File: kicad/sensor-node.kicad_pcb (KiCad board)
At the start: 2 copper layers, 30 x 54 mm, 24 parts

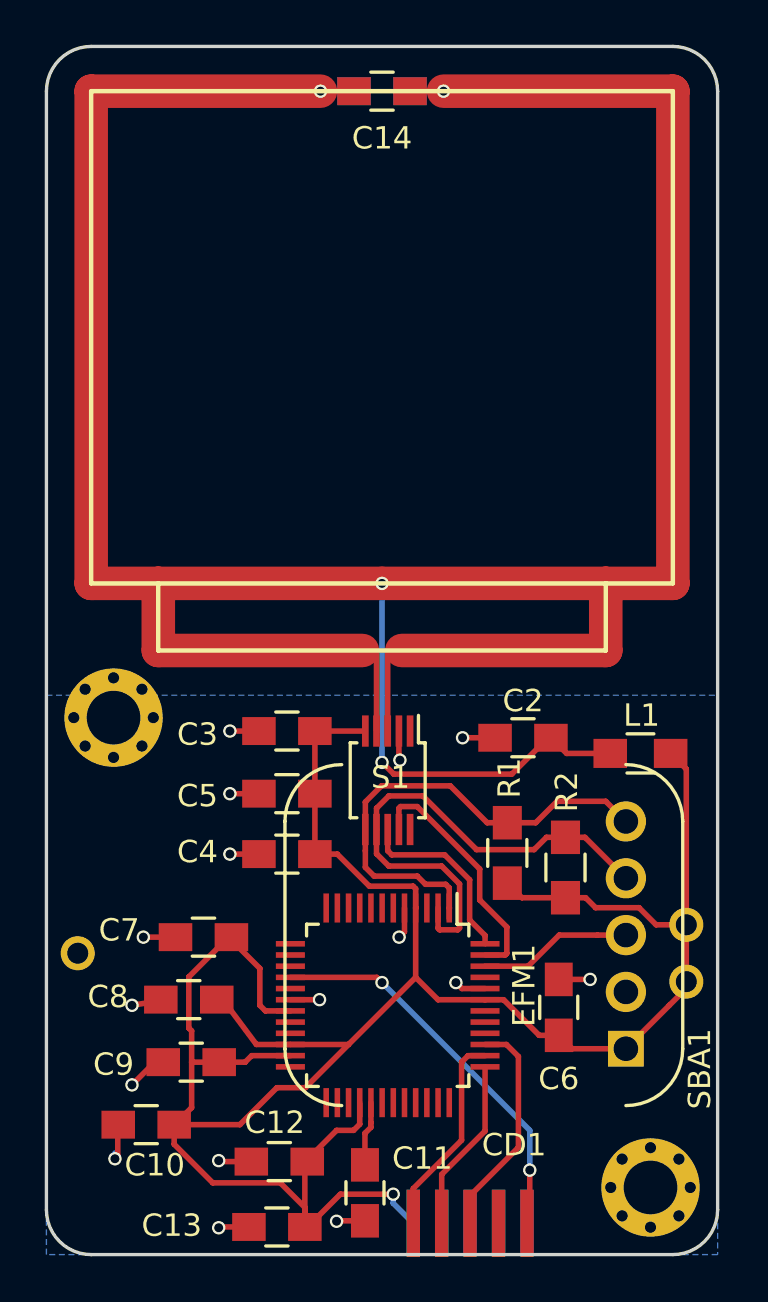
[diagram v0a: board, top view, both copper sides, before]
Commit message: moved cortex debug connector futher to the right
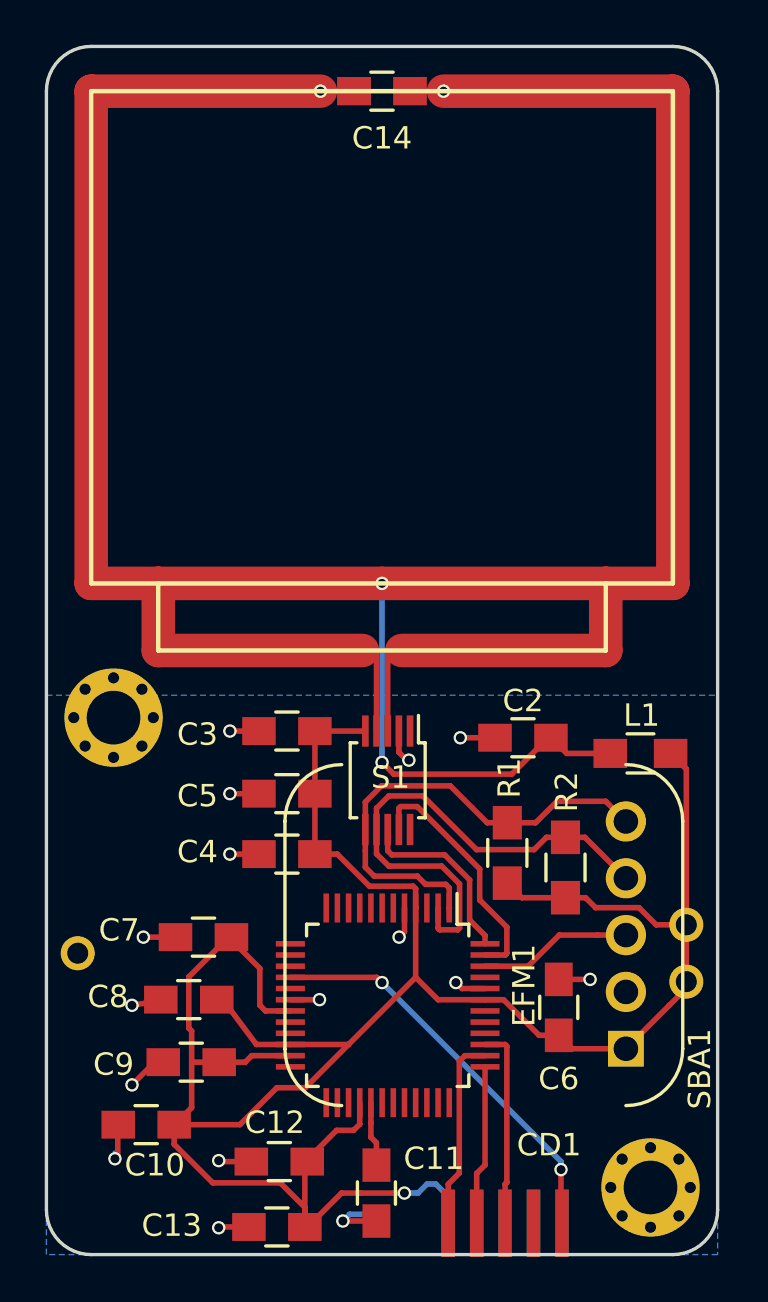
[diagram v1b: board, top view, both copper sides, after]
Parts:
- moved CD1 1.56 mm to (155.1, 110.1)
- moved C11 0.51 mm to (151.9, 108.7)
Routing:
- net +3V3: track 113.5 -> 116.0 mm
- net GND: track 22.9 -> 24.8 mm
- net /SWDIO: track 10.1 -> 8.70 mm
- net /~RESET: track 17.3 -> 18.3 mm
- net /SWO: track 9.85 -> 8.95 mm
- net /SWCLK: track 7.70 -> 7.15 mm

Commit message: moved mounting hole and battery slightliy down
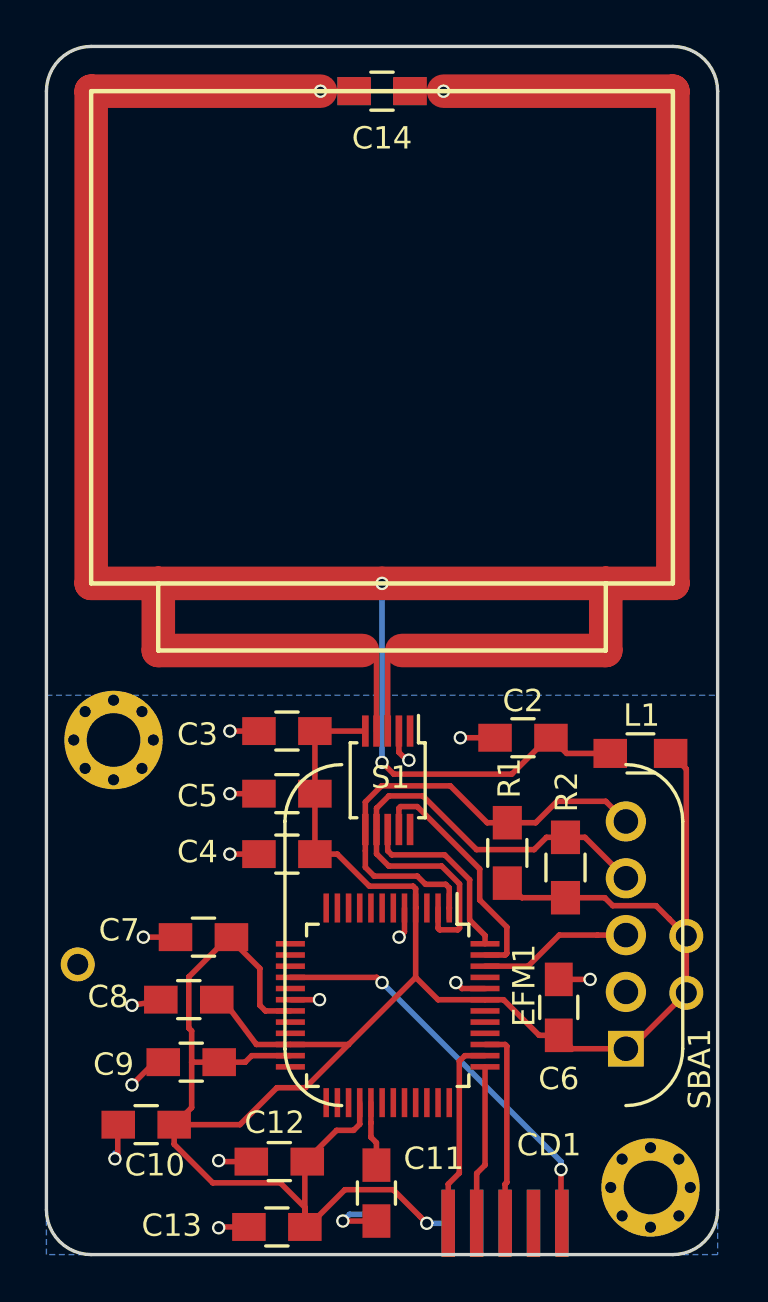
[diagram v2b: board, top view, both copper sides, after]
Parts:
- moved REF** 1.00 mm to (140.1, 88.5)
- moved BT1 0.50 mm to (165.7, 98.5)
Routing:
- net +3V3: track 116.0 -> 115.3 mm
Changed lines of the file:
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@@
     (thickness 1.6)
     (drawings 18)
-    (tracks 242)
+    (tracks 238)
     (zones 0)
     (modules 24)
@@
   )
   (module sensor-node:HU2032-LF (layer B.Cu)
-    (at 165.746 98.001 180)
+    (at 165.746 98.501 180)
     (fp_text reference BT1 (at 13.208 0 180) (layer B.SilkS)
       (effects (font (size 1 1) (thickness 0.15)) (justify mirror))
@@
   )
   (module sensor-node:mounting (layer F.Cu)
-    (at 140.146 87.471)
+    (at 140.146 88.471)
     (fp_text reference REF** (at 0 0.5) (layer F.SilkS) hide
       (effects (font (size 1 1) (thickness 0.15)))
@@
   (gr_line (start 137.146 109.471) (end 137.146 59.471) (layer Edge.Cuts) (width 0.15))
   (gr_line (start 167.146 59.471) (end 167.146 109.471) (layer Edge.Cuts) (width 0.15))
-  (segment (start 153.146 108.721) (end 153.756 108.721) (width 0.25) (layer B.Cu) (net 1))
-  (segment (start 153.756 108.721) (end 154.156 108.321) (width 0.25) (layer B.Cu) (net 1))
-  (segment (start 154.556 108.321) (end 155.106 108.871) (width 0.25) (layer B.Cu) (net 1))
-  (segment (start 154.156 108.321) (end 154.556 108.321) (width 0.25) (layer B.Cu) (net 1))
-  (segment (start 155.106 108.871) (end 155.106 110.071) (width 0.25) (layer B.Cu) (net 1))
-  (segment (start 153.146 108.721) (end 153.216 108.721) (width 0.25) (layer B.Cu) (net 1))
-  (segment (start 148.822 110.236) (end 150.337 108.721) (width 0.25) (layer F.Cu) (net 1))
-  (segment (start 150.337 108.721) (end 151.185998 108.721) (width 0.25) (layer F.Cu) (net 1))
-  (segment (start 151.185998 108.721) (end 153.146 108.721) (width 0.25) (layer F.Cu) (net 1))
-  (via (at 153.146 108.721) (size 0.6) (drill 0.4) (layers F.Cu B.Cu) (net 1))
+  (segment (start 165.746 99.771) (end 165.746 98.69337) (width 0.25) (layer F.Cu) (net 1))
+  (segment (start 165.746 98.69337) (end 165.746 97.231) (width 0.25) (layer F.Cu) (net 1))
+  (segment (start 165.746 99.771) (end 163.246 102.271) (width 0.25) (layer F.Cu) (net 1))
+  (segment (start 163.246 102.271) (end 163.046 102.271) (width 0.25) (layer F.Cu) (net 1))
+  (segment (start 165.746 97.231) (end 165.746 89.771) (width 0.25) (layer F.Cu) (net 1))
+  (segment (start 165.746 89.771) (end 165.046 89.071) (width 0.25) (layer F.Cu) (net 1))
+  (segment (start 160.346 95.521) (end 162.102998 95.521) (width 0.25) (layer F.Cu) (net 1))
+  (segment (start 162.102998 95.521) (end 162.457999 95.876001) (width 0.25) (layer F.Cu) (net 1))
+  (segment (start 162.457999 95.876001) (end 164.391001 95.876001) (width 0.25) (layer F.Cu) (net 1))
+  (segment (start 164.391001 95.876001) (end 164.984001 96.469001) (width 0.25) (layer F.Cu) (net 1))
+  (segment (start 164.984001 96.469001) (end 165.746 97.231) (width 0.25) (layer F.Cu) (net 1))
+  (segment (start 154.146006 110.071) (end 155.106 110.071) (width 0.25) (layer B.Cu) (net 1))
+  (segment (start 153.846007 109.771001) (end 154.146006 110.071) (width 0.25) (layer F.Cu) (net 1))
+  (segment (start 152.645991 108.570985) (end 153.846007 109.771001) (width 0.25) (layer F.Cu) (net 1))
+  (segment (start 150.487015 108.570985) (end 152.645991 108.570985) (width 0.25) (layer F.Cu) (net 1))
+  (segment (start 148.822 110.236) (end 150.487015 108.570985) (width 0.25) (layer F.Cu) (net 1))
+  (segment (start 148.697 110.236) (end 148.822 110.236) (width 0.25) (layer F.Cu) (net 1))
+  (via (at 154.146006 110.071) (size 0.6) (drill 0.4) (layers F.Cu B.Cu) (net 1))
   (segment (start 160.346 95.521) (end 158.398 95.521) (width 0.25) (layer F.Cu) (net 1))
   (segment (start 158.398 95.521) (end 157.746 94.869) (width 0.25) (layer F.Cu) (net 1))
-  (segment (start 165.746 96.731) (end 164.399002 96.731) (width 0.25) (layer F.Cu) (net 1))
-  (segment (start 164.399002 96.731) (end 163.634001 95.965999) (width 0.25) (layer F.Cu) (net 1))
-  (segment (start 163.634001 95.965999) (end 161.690999 95.965999) (width 0.25) (layer F.Cu) (net 1))
-  (segment (start 161.690999 95.965999) (end 161.246 95.521) (width 0.25) (layer F.Cu) (net 1))
-  (segment (start 161.246 95.521) (end 160.346 95.521) (width 0.25) (layer F.Cu) (net 1))
   (segment (start 150.146 93.571) (end 149.146 93.571) (width 0.25) (layer F.Cu) (net 1))
   (segment (start 153.535001 95.004999) (end 151.579999 95.004999) (width 0.25) (layer F.Cu) (net 1))
@@
   (segment (start 153.65 95.98) (end 153.65 95.119998) (width 0.25) (layer F.Cu) (net 1))
   (segment (start 153.65 95.119998) (end 153.535001 95.004999) (width 0.25) (layer F.Cu) (net 1))
-  (segment (start 148.697 110.236) (end 148.822 110.236) (width 0.25) (layer F.Cu) (net 1))
   (segment (start 160.793 95.504) (end 159.893 95.504) (width 0.25) (layer F.Cu) (net 1))
   (segment (start 148.697 110.236) (end 148.697 109.361) (width 0.25) (layer F.Cu) (net 1))
@@
   (segment (start 149.146 90.871) (end 149.146 88.071) (width 0.25) (layer F.Cu) (net 1))
   (segment (start 149.146 93.571) (end 149.146 90.871) (width 0.25) (layer F.Cu) (net 1))
-  (segment (start 165.746 97.031) (end 165.746 89.771) (width 0.25) (layer F.Cu) (net 1))
-  (segment (start 165.746 89.771) (end 165.046 89.071) (width 0.25) (layer F.Cu) (net 1))
-  (segment (start 165.746 99.571) (end 165.746 98.49337) (width 0.25) (layer F.Cu) (net 1))
-  (segment (start 165.746 98.49337) (end 165.746 97.031) (width 0.25) (layer F.Cu) (net 1))
   (segment (start 160.046 101.671) (end 159.171 101.671) (width 0.25) (layer F.Cu) (net 1))
   (segment (start 159.171 101.671) (end 157.58 100.08) (width 0.25) (layer F.Cu) (net 1))
@@
   (segment (start 163.046 102.271) (end 160.646 102.271) (width 0.25) (layer F.Cu) (net 1))
   (segment (start 160.646 102.271) (end 160.046 101.671) (width 0.25) (layer F.Cu) (net 1))
-  (segment (start 165.746 99.571) (end 164.984001 100.332999) (width 0.25) (layer F.Cu) (net 1))
-  (segment (start 164.984001 100.332999) (end 163.046 102.271) (width 0.25) (layer F.Cu) (net 1))
   (segment (start 144.867 102.87) (end 143.637 102.87) (width 0.25) (layer F.Cu) (net 1))
   (segment (start 146.03 102.87) (end 144.867 102.87) (width 0.25) (layer F.Cu) (net 1))

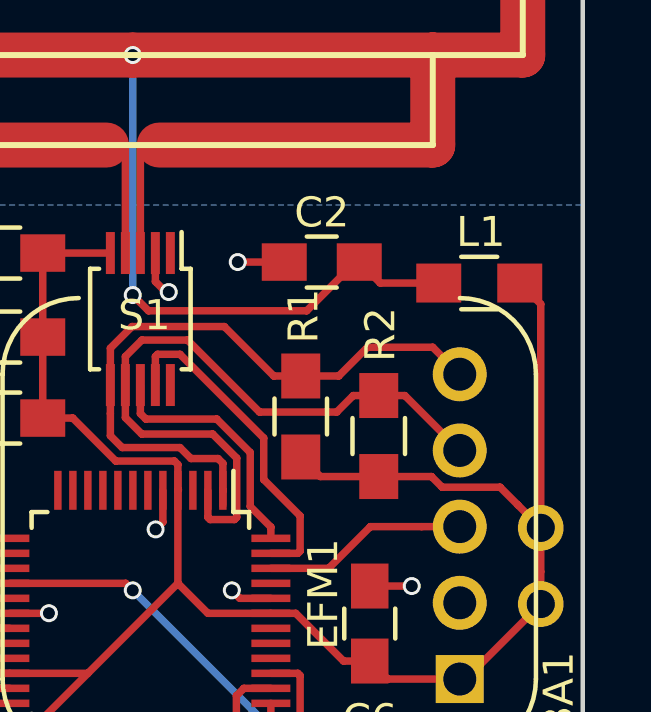
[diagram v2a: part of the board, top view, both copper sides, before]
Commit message: moved inductivity up
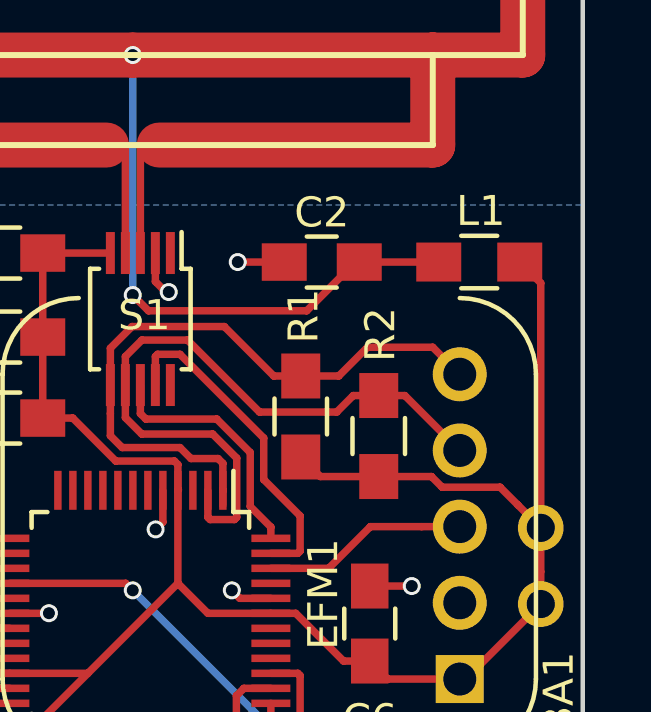
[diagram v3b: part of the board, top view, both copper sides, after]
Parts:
- moved L1 0.70 mm to (163.7, 88.4)
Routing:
- net +3V3: track 115.3 -> 116.0 mm
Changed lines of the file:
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@@
     (links 81)
     (no_connects 0)
-    (area 124.24918 56.396 179.995999 119.171001)
+    (area 137.070999 57.395999 167.221001 111.546001)
     (thickness 1.6)
     (drawings 18)
-    (tracks 238)
+    (tracks 237)
     (zones 0)
     (modules 24)
@@
   )
   (module Resistors_SMD:R_0805_HandSoldering (layer F.Cu)
-    (at 163.696 89.071 180)
+    (at 163.696 88.371 180)
     (descr "Resistor SMD 0805, hand soldering")
     (tags "resistor 0805")
@@
   (gr_line (start 137.146 109.471) (end 137.146 59.471) (layer Edge.Cuts) (width 0.15))
   (gr_line (start 167.146 59.471) (end 167.146 109.471) (layer Edge.Cuts) (width 0.15))
+  (segment (start 165.746 97.231) (end 165.746 89.071) (width 0.25) (layer F.Cu) (net 1))
+  (segment (start 165.746 89.071) (end 165.046 88.371) (width 0.25) (layer F.Cu) (net 1))
   (segment (start 165.746 99.771) (end 165.746 98.69337) (width 0.25) (layer F.Cu) (net 1))
   (segment (start 165.746 98.69337) (end 165.746 97.231) (width 0.25) (layer F.Cu) (net 1))
   (segment (start 165.746 99.771) (end 163.246 102.271) (width 0.25) (layer F.Cu) (net 1))
   (segment (start 163.246 102.271) (end 163.046 102.271) (width 0.25) (layer F.Cu) (net 1))
-  (segment (start 165.746 97.231) (end 165.746 89.771) (width 0.25) (layer F.Cu) (net 1))
-  (segment (start 165.746 89.771) (end 165.046 89.071) (width 0.25) (layer F.Cu) (net 1))
   (segment (start 160.346 95.521) (end 162.102998 95.521) (width 0.25) (layer F.Cu) (net 1))
   (segment (start 162.102998 95.521) (end 162.457999 95.876001) (width 0.25) (layer F.Cu) (net 1))
@@
   (segment (start 142.367 102.87) (end 141.986 102.87) (width 0.25) (layer F.Cu) (net 2))
   (segment (start 141.986 102.87) (end 140.97 103.886) (width 0.25) (layer F.Cu) (net 2))
+  (segment (start 162.346 88.371) (end 159.696 88.371) (width 0.25) (layer F.Cu) (net 3))
   (segment (start 152.4 84.475) (end 153.025 84.475) (width 0.25) (layer F.Cu) (net 3))
   (segment (start 153.025 84.475) (end 153.029 84.471) (width 0.25) (layer F.Cu) (net 3))
@@
   (segment (start 151.9 84.475) (end 151.896 84.471) (width 0.25) (layer F.Cu) (net 3))
   (segment (start 151.9 88.071) (end 151.9 84.475) (width 0.25) (layer F.Cu) (net 3))
-  (segment (start 162.346 89.071) (end 160.396 89.071) (width 0.25) (layer F.Cu) (net 3))
-  (segment (start 160.396 89.071) (end 159.696 88.371) (width 0.25) (layer F.Cu) (net 3))
   (segment (start 151.896 107.471) (end 151.896 106.471) (width 0.25) (layer F.Cu) (net 4))
   (segment (start 151.896 106.471) (end 151.65 106.225) (width 0.25) (layer F.Cu) (net 4))

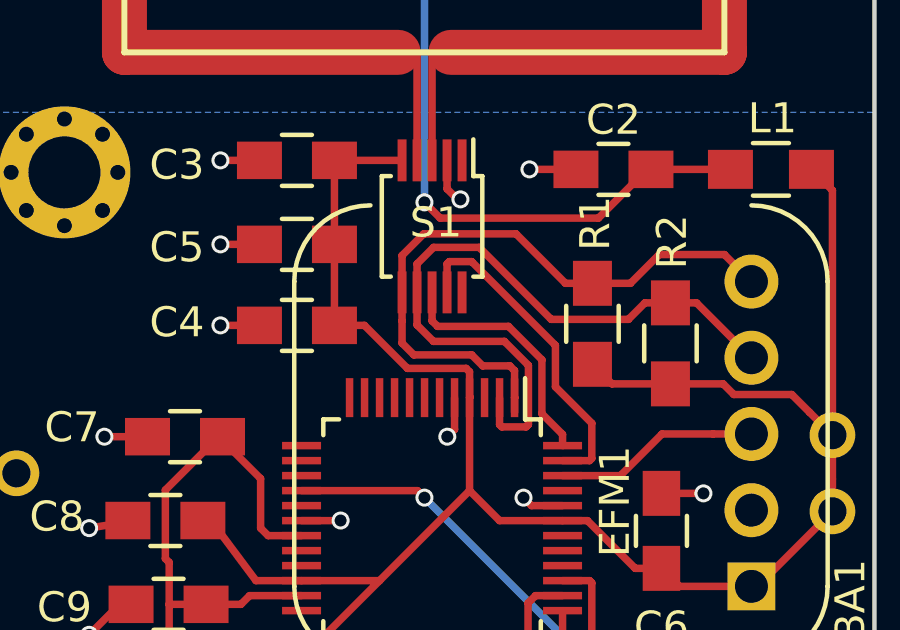
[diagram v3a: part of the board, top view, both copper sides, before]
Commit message: check i2c connections
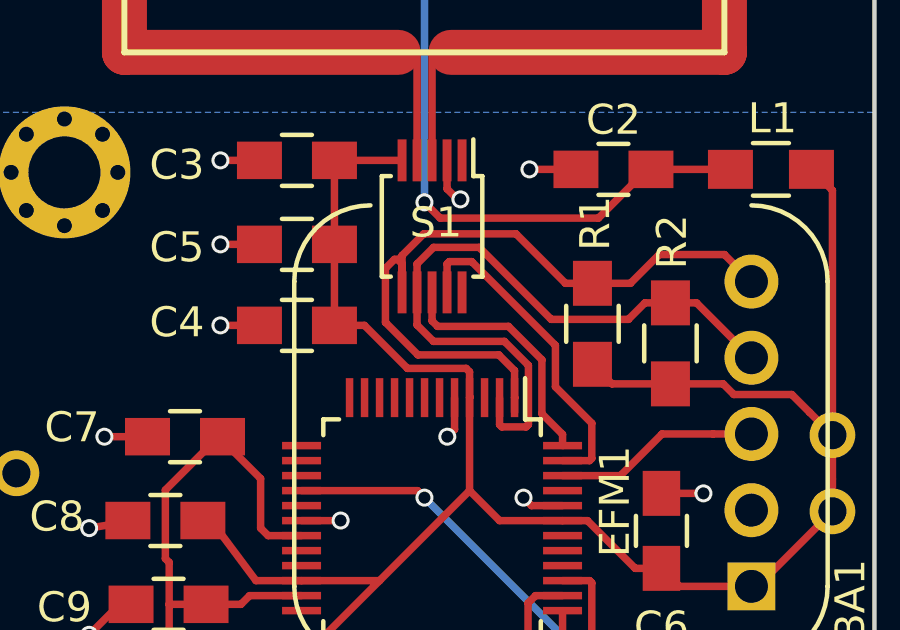
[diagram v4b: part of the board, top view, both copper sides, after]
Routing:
- net /SDA: track 22.8 -> 25.4 mm
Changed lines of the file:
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@@
     (links 81)
     (no_connects 0)
-    (area 137.070999 57.395999 167.221001 111.546001)
+    (area 124.24918 56.396 179.995999 119.171001)
     (thickness 1.6)
     (drawings 18)
-    (tracks 237)
+    (tracks 238)
     (zones 0)
     (modules 24)
@@
   (via (at 152.146 99.314) (size 0.6) (drill 0.4) (layers F.Cu B.Cu) (net 8))
   (segment (start 148.05 99.08) (end 151.912 99.08) (width 0.25) (layer F.Cu) (net 8))
+  (segment (start 151.146 91.371) (end 151.25 91.371) (width 0.25) (layer F.Cu) (net 9))
+  (segment (start 151.25 91.371) (end 151.4 91.521) (width 0.25) (layer F.Cu) (net 9))
+  (segment (start 151.4 91.521) (end 151.4 92.471) (width 0.25) (layer F.Cu) (net 9))
+  (segment (start 150.846 91.671) (end 151.146 91.371) (width 0.25) (layer F.Cu) (net 9))
+  (segment (start 155.15 95.98) (end 155.15 95.08) (width 0.25) (layer F.Cu) (net 9))
+  (segment (start 155.15 95.08) (end 154.624989 94.554989) (width 0.25) (layer F.Cu) (net 9))
+  (segment (start 154.624989 94.554989) (end 151.929989 94.554989) (width 0.25) (layer F.Cu) (net 9))
+  (segment (start 151.929989 94.554989) (end 150.846 93.471) (width 0.25) (layer F.Cu) (net 9))
+  (segment (start 150.846 93.471) (end 150.846 91.671) (width 0.25) (layer F.Cu) (net 9))
   (segment (start 157.746 92.169) (end 159.012998 92.169) (width 0.25) (layer F.Cu) (net 9))
   (segment (start 159.012998 92.169) (end 159.970997 91.211001) (width 0.25) (layer F.Cu) (net 9))
@@
   (segment (start 155.197991 90.520991) (end 156.846 92.169) (width 0.25) (layer F.Cu) (net 9))
   (segment (start 156.846 92.169) (end 157.746 92.169) (width 0.25) (layer F.Cu) (net 9))
-  (segment (start 151.793577 94.554988) (end 151.4 94.161411) (width 0.25) (layer F.Cu) (net 9))
-  (segment (start 154.087424 94.921011) (end 153.721401 94.554988) (width 0.25) (layer F.Cu) (net 9))
-  (segment (start 155.15 95.98) (end 155.15 95.08) (width 0.25) (layer F.Cu) (net 9))
-  (segment (start 151.4 93.421) (end 151.4 92.471) (width 0.25) (layer F.Cu) (net 9))
-  (segment (start 154.991011 94.921011) (end 154.087424 94.921011) (width 0.25) (layer F.Cu) (net 9))
-  (segment (start 153.721401 94.554988) (end 151.793577 94.554988) (width 0.25) (layer F.Cu) (net 9))
-  (segment (start 155.15 95.08) (end 154.991011 94.921011) (width 0.25) (layer F.Cu) (net 9))
-  (segment (start 151.4 94.161411) (end 151.4 93.421) (width 0.25) (layer F.Cu) (net 9))
   (segment (start 157.353 92.169) (end 158.253 92.169) (width 0.25) (layer F.Cu) (net 9))
   (segment (start 155.15 95.98) (end 155.162 95.98) (width 0.25) (layer F.Cu) (net 9))
